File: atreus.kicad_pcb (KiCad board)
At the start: 2 copper layers, 139.7 x 101.6 mm, 45 parts

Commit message: c
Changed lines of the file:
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@@
     (mod_text_size 1.524 1.524)
     (mod_text_width 0.3048)
-    (pad_size 2.5 1.651)
-    (pad_drill 0.9906)
+    (pad_size 3.032 1.7272)
+    (pad_drill 1.016)
     (pad_to_mask_clearance 0.254)
     (aux_axis_origin 0 0)
@@
   (segment (start 144.78 63.5) (end 149.86 63.5) (width 0.5) (layer Front) (net 0))
   (segment (start 144.78 60.96) (end 149.86 60.96) (width 0.5) (layer Front) (net 0))
-  (segment (start 144.78 58.42) (end 149.86 58.42) (width 0.6) (layer Front) (net 0))
+  (segment (start 144.78 58.42) (end 149.86 58.42) (width 0.5) (layer Front) (net 0))
   (segment (start 124 37.005) (end 125.095 38.1) (width 0.5) (layer Front) (net 1))
   (segment (start 125.095 38.1) (end 129.54 38.1) (width 0.5) (layer Front) (net 1))

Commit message: more nets, a hole
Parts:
- added REF**: MountingHole_5mm, Mounting_Holes:MountingHole_5mm, F.Cu at (25.4, 12.7)
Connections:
- REF** pad 11: (no net) -> N-i2c-scl
- REF** pad 12: (no net) -> N-i2c-sda
- REF** pad 13: (no net) -> N-GND
- REF** pad 14: (no net) -> N-VCC
- REF** pad 1: (no net) -> N-i2c-scl
- REF** pad 2: (no net) -> N-i2c-sda
- REF** pad 3: (no net) -> N-GND
- REF** pad 4: (no net) -> N-VCC
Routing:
- net (no net): track 20.3 -> 0.00 mm
- net N-i2c-sda: track 0.00 -> 5.08 mm
- net N-i2c-scl: track 0.00 -> 5.08 mm
- net N-VCC: track 0.00 -> 5.08 mm
- net N-GND: track 0.00 -> 5.08 mm
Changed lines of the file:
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@@
     (tracks 297)
     (zones 0)
-    (modules 45)
-    (nets 32)
+    (modules 46)
+    (nets 36)
   )
   (page A4)
@@
   (net 30 N-diode-19)
   (net 31 N-diode-20)
+  (net 32 N-VCC)
+  (net 33 N-GND)
+  (net 34 N-i2c-scl)
+  (net 35 N-i2c-sda)
   (net_class Default "This is the default net class."
     (clearance 0.8)
@@
     (pad 9 thru_hole oval (at 0 20.32) (size 3.032 1.7272) (drill 1.016) (layers *.Cu *.Mask F.SilkS))
     (pad 10 thru_hole oval (at 0 22.86) (size 3.032 1.7272) (drill 1.016) (layers *.Cu *.Mask F.SilkS))
-    (pad 11 thru_hole oval (at 0 25.4) (size 3.032 1.7272) (drill 1.016) (layers *.Cu *.Mask F.SilkS))
-    (pad 12 thru_hole oval (at 0 27.94) (size 3.032 1.7272) (drill 1.016) (layers *.Cu *.Mask F.SilkS))
-    (pad 13 thru_hole oval (at 0 30.48) (size 3.032 1.7272) (drill 1.016) (layers *.Cu *.Mask F.SilkS))
-    (pad 14 thru_hole oval (at 0 33.02) (size 3.032 1.7272) (drill 1.016) (layers *.Cu *.Mask F.SilkS))
+    (pad 11 thru_hole oval (at 0 25.4) (size 3.032 1.7272) (drill 1.016) (layers *.Cu *.Mask F.SilkS)
+      (net 34 N-i2c-scl))
+    (pad 12 thru_hole oval (at 0 27.94) (size 3.032 1.7272) (drill 1.016) (layers *.Cu *.Mask F.SilkS)
+      (net 35 N-i2c-sda))
+    (pad 13 thru_hole oval (at 0 30.48) (size 3.032 1.7272) (drill 1.016) (layers *.Cu *.Mask F.SilkS)
+      (net 33 N-GND))
+    (pad 14 thru_hole oval (at 0 33.02) (size 3.032 1.7272) (drill 1.016) (layers *.Cu *.Mask F.SilkS)
+      (net 32 N-VCC))
     (model Pin_Headers.3dshapes/Pin_Header_Straight_1x14.wrl
       (at (xyz 0 -0.65 0))
@@
     (fp_line (start -1.55 0) (end -1.55 -1.55) (layer F.SilkS) (width 0.15))
     (fp_line (start -1.55 -1.55) (end 1.55 -1.55) (layer F.SilkS) (width 0.15))
-    (pad 1 thru_hole rect (at 0 0) (size 3.032 1.7272) (drill 1.016) (layers *.Cu *.Mask F.SilkS))
-    (pad 2 thru_hole oval (at 0 2.54) (size 3.032 1.7272) (drill 1.016) (layers *.Cu *.Mask F.SilkS))
-    (pad 3 thru_hole oval (at 0 5.08) (size 3.032 1.7272) (drill 1.016) (layers *.Cu *.Mask F.SilkS))
-    (pad 4 thru_hole oval (at 0 7.62) (size 3.032 1.7272) (drill 1.016) (layers *.Cu *.Mask F.SilkS))
+    (pad 1 thru_hole rect (at 0 0) (size 3.032 1.7272) (drill 1.016) (layers *.Cu *.Mask F.SilkS)
+      (net 34 N-i2c-scl))
+    (pad 2 thru_hole oval (at 0 2.54) (size 3.032 1.7272) (drill 1.016) (layers *.Cu *.Mask F.SilkS)
+      (net 35 N-i2c-sda))
+    (pad 3 thru_hole oval (at 0 5.08) (size 3.032 1.7272) (drill 1.016) (layers *.Cu *.Mask F.SilkS)
+      (net 33 N-GND))
+    (pad 4 thru_hole oval (at 0 7.62) (size 3.032 1.7272) (drill 1.016) (layers *.Cu *.Mask F.SilkS)
+      (net 32 N-VCC))
     (model Pin_Headers.3dshapes/Pin_Header_Straight_1x04.wrl
       (at (xyz 0 -0.15 0))
@@
       (rotate (xyz 0 0 90))
     )
+  )
+  (module Mounting_Holes:MountingHole_5mm (layer Front)
+    (at 25.4 12.7)
+    (descr "Mounting hole, Befestigungsbohrung, 5mm, No Annular, Kein Restring,")
+    (tags "Mounting hole, Befestigungsbohrung, 5mm, No Annular, Kein Restring,")
+    (fp_text reference REF** (at 0 -6.49986) (layer F.SilkS)
+      (effects (font (size 1 1) (thickness 0.15)))
+    )
+    (fp_text value MountingHole_5mm (at 0 7.00024) (layer F.Fab)
+      (effects (font (size 1 1) (thickness 0.15)))
+    )
+    (fp_circle (center 0 0) (end 5 0) (layer Cmts.User) (width 0.381))
+    (pad 1 thru_hole circle (at 0 0) (size 5 5) (drill 5) (layers))
   )
   (dimension 101.6 (width 0.3048) (layer F.SilkS)
@@
   (gr_line (start 154.94 5.08) (end 157.48 5.08) (layer Edge.Cuts) (width 0.381))
   (gr_line (start 17.78 5.08) (end 154.94 5.08) (layer Edge.Cuts) (width 0.381))
-  (segment (start 144.78 66.04) (end 149.86 66.04) (width 0.5) (layer Front) (net 0))
-  (segment (start 144.78 63.5) (end 149.86 63.5) (width 0.5) (layer Front) (net 0))
-  (segment (start 144.78 60.96) (end 149.86 60.96) (width 0.5) (layer Front) (net 0))
-  (segment (start 144.78 58.42) (end 149.86 58.42) (width 0.5) (layer Front) (net 0))
   (segment (start 124 37.005) (end 125.095 38.1) (width 0.5) (layer Front) (net 1))
   (segment (start 125.095 38.1) (end 129.54 38.1) (width 0.5) (layer Front) (net 1))
@@
   (segment (start 131.46 75.19) (end 130.19 75.19) (width 0.5) (layer Front) (net 31))
   (segment (start 130.19 75.19) (end 128.92 76.46) (width 0.5) (layer Front) (net 31))
+  (segment (start 144.78 66.04) (end 149.86 66.04) (width 0.5) (layer Front) (net 32))
+  (segment (start 144.78 63.5) (end 149.86 63.5) (width 0.5) (layer Front) (net 33))
+  (segment (start 144.78 58.42) (end 149.86 58.42) (width 0.5) (layer Front) (net 34))
+  (segment (start 144.78 60.96) (end 149.86 60.96) (width 0.5) (layer Front) (net 35))
 )

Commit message: fills
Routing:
- net N-GND: track 5.08 -> 16.5 mm, vias 0 -> 1
- net (no net): vias 0 -> 1
- added copper zone on B.Cu, net N-GND
- added copper zone on F.Cu, net N-GND
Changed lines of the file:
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@@
 (kicad_pcb (version 4) (host pcbnew 4.0.2-stable)
   (general
-    (links 105)
+    (links 109)
     (no_connects 0)
     (area -3.265715 -6.0452 160.449287 106.870501)
     (thickness 1.6002)
     (drawings 7)
-    (tracks 297)
+    (tracks 301)
     (zones 0)
     (modules 46)
@@
     (last_trace_width 0.5)
     (trace_clearance 0.8)
-    (zone_clearance 0.508)
+    (zone_clearance 1.5)
     (zone_45_only no)
     (trace_min 0.2032)
@@
     (uvia_dia 0.508)
     (uvia_drill 0.127)
+    (add_net N-GND)
+    (add_net N-VCC)
     (add_net N-col-0)
     (add_net N-col-1)
@@
     (add_net N-diode-8)
     (add_net N-diode-9)
+    (add_net N-i2c-scl)
+    (add_net N-i2c-sda)
     (add_net N-row-0)
     (add_net N-row-1)
@@
   (gr_line (start 154.94 5.08) (end 157.48 5.08) (layer Edge.Cuts) (width 0.381))
   (gr_line (start 17.78 5.08) (end 154.94 5.08) (layer Edge.Cuts) (width 0.381))
+  (via (at 153.67 81.28) (size 0.889) (drill 0.635) (layers Front Back) (net 0))
   (segment (start 124 37.005) (end 125.095 38.1) (width 0.5) (layer Front) (net 1))
   (segment (start 125.095 38.1) (end 129.54 38.1) (width 0.5) (layer Front) (net 1))
@@
   (segment (start 130.19 75.19) (end 128.92 76.46) (width 0.5) (layer Front) (net 31))
   (segment (start 144.78 66.04) (end 149.86 66.04) (width 0.5) (layer Front) (net 32))
+  (segment (start 149.86 63.5) (end 153.67 63.5) (width 0.5) (layer Front) (net 33))
+  (via (at 153.67 71.12) (size 0.889) (drill 0.635) (layers Front Back) (net 33))
+  (segment (start 153.67 63.5) (end 153.67 71.12) (width 0.5) (layer Front) (net 33))
   (segment (start 144.78 63.5) (end 149.86 63.5) (width 0.5) (layer Front) (net 33))
   (segment (start 144.78 58.42) (end 149.86 58.42) (width 0.5) (layer Front) (net 34))
   (segment (start 144.78 60.96) (end 149.86 60.96) (width 0.5) (layer Front) (net 35))
+  (zone (net 33) (net_name N-GND) (layer Front) (hatch edge 0.508)
+    (connect_pads (clearance 1.5))
+    (min_thickness 0.3)
+    (fill yes (arc_segments 16) (thermal_gap 0.508) (thermal_bridge_width 0.508))
+    (polygon
+      (pts
+        (xy 17.78 5.08) (xy 157.48 5.08) (xy 157.48 106.68) (xy 17.78 106.68)
+      )
+    )
+  )
+  (zone (net 33) (net_name N-GND) (layer Back) (hatch edge 0.508)
+    (connect_pads (clearance 1.5))
+    (min_thickness 0.3)
+    (fill yes (arc_segments 16) (thermal_gap 0.508) (thermal_bridge_width 0.508))
+    (polygon
+      (pts
+        (xy 17.78 5.08) (xy 157.48 5.08) (xy 157.48 106.68) (xy 17.78 106.68)
+      )
+    )
+  )
 )

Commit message: render
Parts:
- added REF**: MountingHole_5mm, Mounting_Holes:MountingHole_5mm, F.Cu at (25.4, 99.1)
- added REF**: MountingHole_5mm, Mounting_Holes:MountingHole_5mm, F.Cu at (149.9, 12.7)
- added REF**: MountingHole_5mm, Mounting_Holes:MountingHole_5mm, F.Cu at (149.9, 99.1)
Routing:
- net N-GND: track 16.5 -> 13.0 mm, vias 1 -> 0
- net (no net): vias 1 -> 0
- added copper zone on B.Cu, net (none)
- added copper zone on F.Cu, net (none)
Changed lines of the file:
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@@
 (kicad_pcb (version 4) (host pcbnew 4.0.2-stable)
   (general
-    (links 109)
+    (links 0)
     (no_connects 0)
-    (area -3.265715 -6.0452 160.449287 106.870501)
+    (area -3.265715 -6.0452 160.449287 109.220001)
     (thickness 1.6002)
     (drawings 7)
-    (tracks 301)
+    (tracks 299)
     (zones 0)
-    (modules 46)
+    (modules 49)
     (nets 36)
   )
@@
     (last_trace_width 0.5)
     (trace_clearance 0.8)
-    (zone_clearance 1.5)
+    (zone_clearance 1.6)
     (zone_45_only no)
     (trace_min 0.2032)
@@
     (visible_elements FFFFFF7F)
     (pcbplotparams
-      (layerselection 0x00030_80000001)
-      (usegerberextensions true)
+      (layerselection 0x00000_80000001)
+      (usegerberextensions false)
       (excludeedgelayer true)
       (linewidth 0.150000)
@@
       (psnegative false)
       (psa4output false)
-      (plotreference true)
-      (plotvalue true)
+      (plotreference false)
+      (plotvalue false)
       (plotinvisibletext false)
       (padsonsilk false)
@@
       (outputformat 1)
       (mirror false)
-      (drillshape 1)
+      (drillshape 0)
       (scaleselection 1)
       (outputdirectory ""))
@@
     (pad 1 thru_hole circle (at 0 0) (size 5 5) (drill 5) (layers))
   )
+  (module Mounting_Holes:MountingHole_5mm (layer Front)
+    (at 25.4 99.06)
+    (descr "Mounting hole, Befestigungsbohrung, 5mm, No Annular, Kein Restring,")
+    (tags "Mounting hole, Befestigungsbohrung, 5mm, No Annular, Kein Restring,")
+    (fp_text reference REF** (at 0 -6.49986) (layer F.SilkS)
+      (effects (font (size 1 1) (thickness 0.15)))
+    )
+    (fp_text value MountingHole_5mm (at 0 7.00024) (layer F.Fab)
+      (effects (font (size 1 1) (thickness 0.15)))
+    )
+    (fp_circle (center 0 0) (end 5 0) (layer Cmts.User) (width 0.381))
+    (pad 1 thru_hole circle (at 0 0) (size 5 5) (drill 5) (layers))
+  )
+  (module Mounting_Holes:MountingHole_5mm (layer Front)
+    (at 149.86 12.7)
+    (descr "Mounting hole, Befestigungsbohrung, 5mm, No Annular, Kein Restring,")
+    (tags "Mounting hole, Befestigungsbohrung, 5mm, No Annular, Kein Restring,")
+    (fp_text reference REF** (at 0 -6.49986) (layer F.SilkS)
+      (effects (font (size 1 1) (thickness 0.15)))
+    )
+    (fp_text value MountingHole_5mm (at 0 7.00024) (layer F.Fab)
+      (effects (font (size 1 1) (thickness 0.15)))
+    )
+    (fp_circle (center 0 0) (end 5 0) (layer Cmts.User) (width 0.381))
+    (pad 1 thru_hole circle (at 0 0) (size 5 5) (drill 5) (layers))
+  )
+  (module Mounting_Holes:MountingHole_5mm (layer Front)
+    (at 149.86 99.06)
+    (descr "Mounting hole, Befestigungsbohrung, 5mm, No Annular, Kein Restring,")
+    (tags "Mounting hole, Befestigungsbohrung, 5mm, No Annular, Kein Restring,")
+    (fp_text reference REF** (at 0 -6.49986) (layer F.SilkS)
+      (effects (font (size 1 1) (thickness 0.15)))
+    )
+    (fp_text value MountingHole_5mm (at 0 7.00024) (layer F.Fab)
+      (effects (font (size 1 1) (thickness 0.15)))
+    )
+    (fp_circle (center 0 0) (end 5 0) (layer Cmts.User) (width 0.381))
+    (pad 1 thru_hole circle (at 0 0) (size 5 5) (drill 5) (layers))
+  )
   (dimension 101.6 (width 0.3048) (layer F.SilkS)
     (gr_text "101.600 mm / 4 in" (at 8.5344 55.88 270) (layer F.SilkS)
@@
   (gr_line (start 154.94 5.08) (end 157.48 5.08) (layer Edge.Cuts) (width 0.381))
   (gr_line (start 17.78 5.08) (end 154.94 5.08) (layer Edge.Cuts) (width 0.381))
-  (via (at 153.67 81.28) (size 0.889) (drill 0.635) (layers Front Back) (net 0))
   (segment (start 124 37.005) (end 125.095 38.1) (width 0.5) (layer Front) (net 1))
   (segment (start 125.095 38.1) (end 129.54 38.1) (width 0.5) (layer Front) (net 1))
@@
   (segment (start 130.19 75.19) (end 128.92 76.46) (width 0.5) (layer Front) (net 31))
   (segment (start 144.78 66.04) (end 149.86 66.04) (width 0.5) (layer Front) (net 32))
+  (segment (start 149.86 63.5) (end 153.924 63.5) (width 0.5) (layer Front) (net 33))
   (segment (start 149.86 63.5) (end 153.67 63.5) (width 0.5) (layer Front) (net 33))
-  (via (at 153.67 71.12) (size 0.889) (drill 0.635) (layers Front Back) (net 33))
-  (segment (start 153.67 63.5) (end 153.67 71.12) (width 0.5) (layer Front) (net 33))
   (segment (start 144.78 63.5) (end 149.86 63.5) (width 0.5) (layer Front) (net 33))
   (segment (start 144.78 58.42) (end 149.86 58.42) (width 0.5) (layer Front) (net 34))
@@
       )
     )
+  )
+  (zone (net 0) (net_name "") (layer Front) (hatch edge 0.508)
+    (connect_pads (clearance 1.6))
+    (min_thickness 0.3)
+    (fill yes (arc_segments 16) (thermal_gap 0.508) (thermal_bridge_width 0.508))
+    (polygon
+      (pts
+        (xy 17.78 5.08) (xy 157.48 5.08) (xy 157.48 106.68) (xy 17.78 106.68)
+      )
+    )
+  )
+  (zone (net 0) (net_name "") (layer Back) (hatch edge 0.508)
+    (connect_pads (clearance 1.6))
+    (min_thickness 0.3)
+    (fill yes (arc_segments 16) (thermal_gap 0.508) (thermal_bridge_width 0.508))
+    (polygon
+      (pts
+        (xy 17.78 5.08) (xy 157.48 5.08) (xy 157.48 109.22) (xy 157.48 106.68) (xy 17.78 106.68)
+      )
+    )

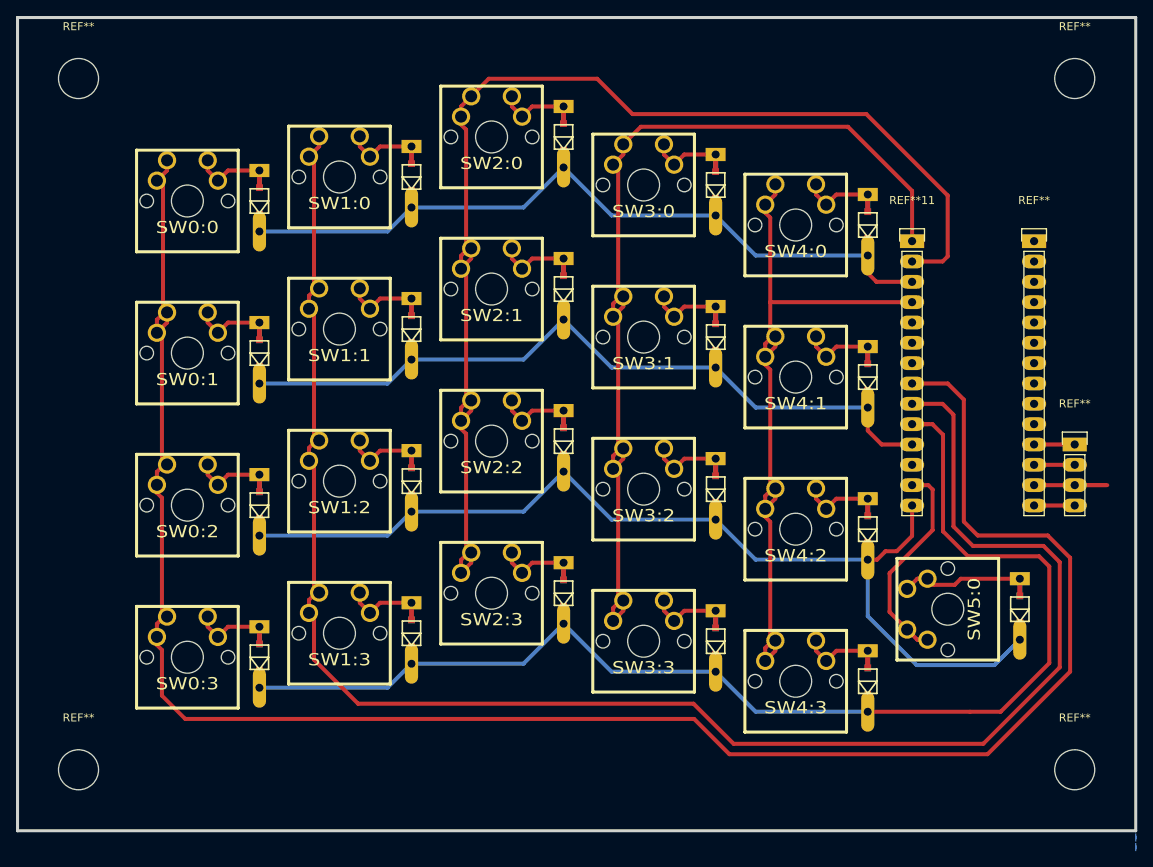
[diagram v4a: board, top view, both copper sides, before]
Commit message: make switch pads oval
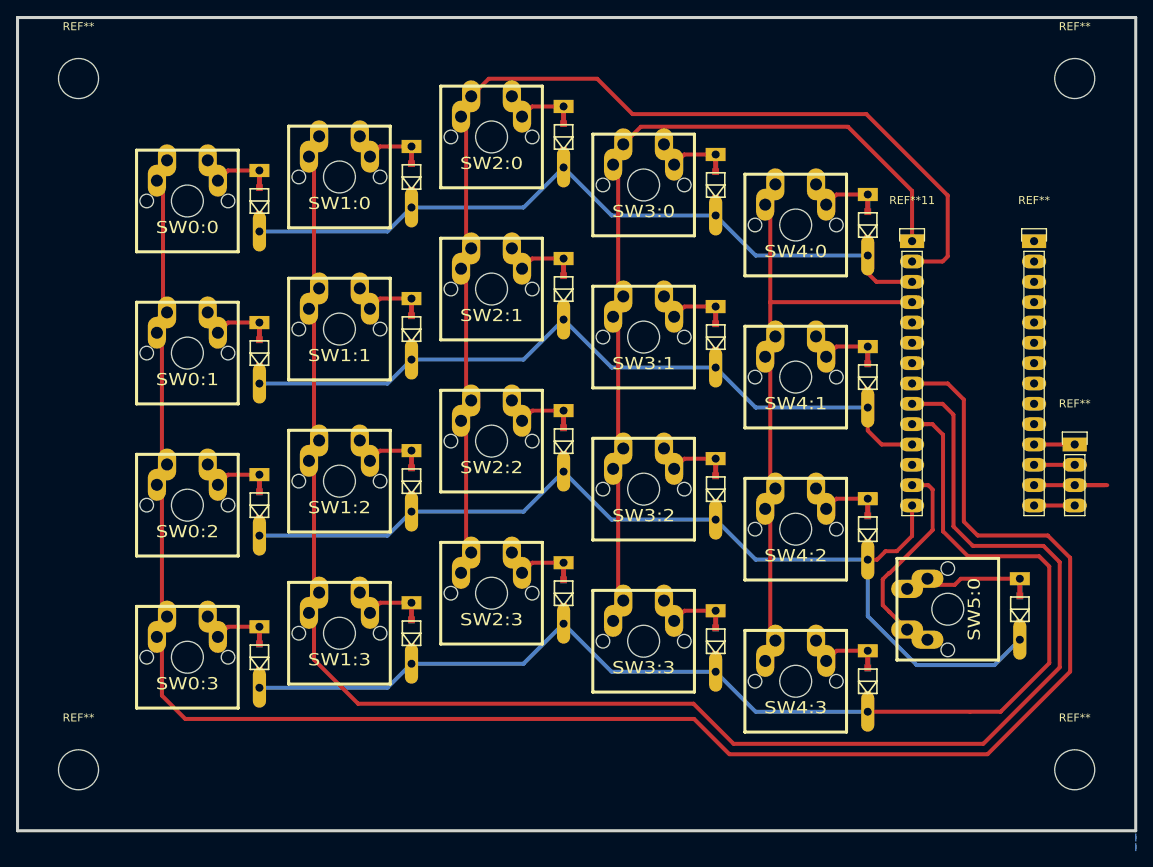
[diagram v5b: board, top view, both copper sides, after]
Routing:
- net N-col-5: track 26.5 -> 27.2 mm
